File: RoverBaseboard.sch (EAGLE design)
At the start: 57 parts, among them IC3 3.3V, U2 microSD

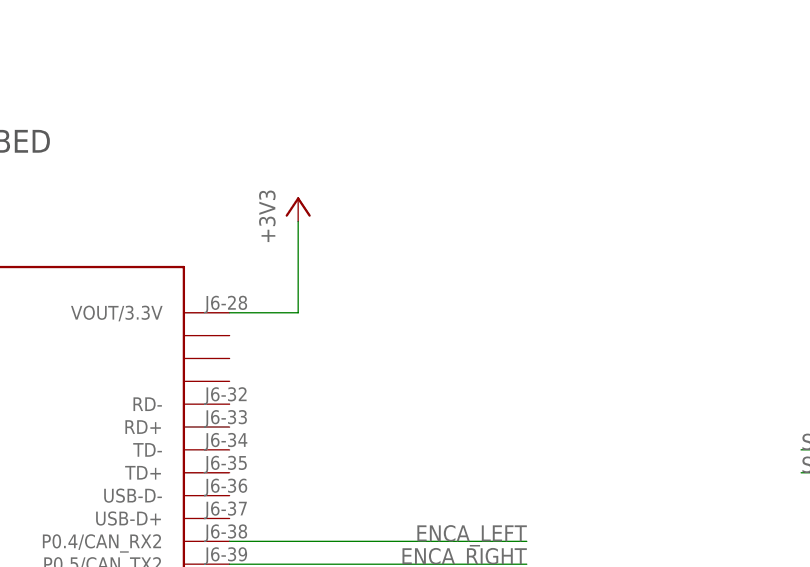
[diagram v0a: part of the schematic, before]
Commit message: added diode for VUSB/5V so both can be connected safely
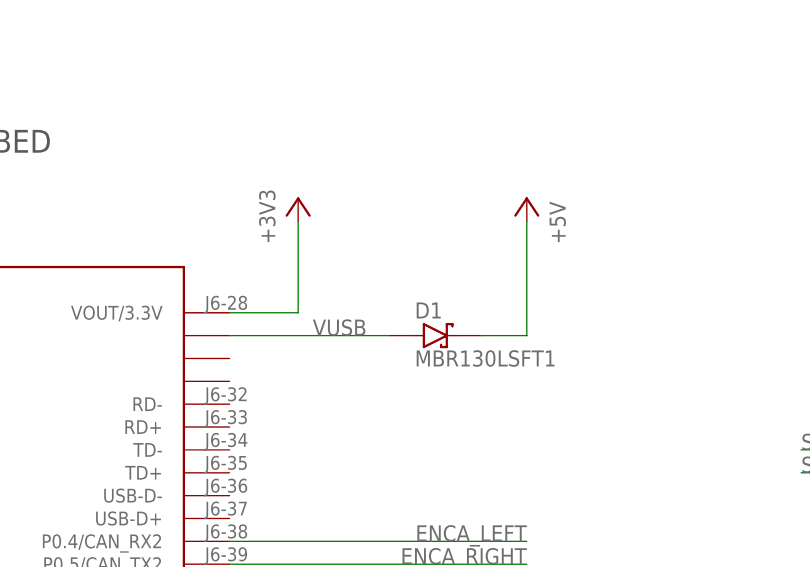
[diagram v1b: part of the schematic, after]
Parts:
- added D1: MBR130LSFT1, bt_diode:SCHOTTKY-DIODE-MBR130LSFT1
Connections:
- new net VUSB: D1.A, U$1.P$26
- net +5V: now also D1.C
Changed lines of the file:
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@@
 <?xml version="1.0" encoding="utf-8"?>
 <!DOCTYPE eagle SYSTEM "eagle.dtd">
-<eagle version="6.4">
+<eagle version="7.1.0">
 <drawing>
 <settings>
@@
 <grid distance="0.1" unitdist="inch" unit="inch" style="lines" multiple="1" display="no" altdistance="0.01" altunitdist="inch" altunit="inch"/>
 <layers>
-<layer number="1" name="Top" color="4" fill="1" visible="yes" active="no"/>
-<layer number="16" name="Bottom" color="1" fill="1" visible="yes" active="no"/>
-<layer number="17" name="Pads" color="2" fill="1" visible="yes" active="no"/>
-<layer number="18" name="Vias" color="2" fill="1" visible="yes" active="no"/>
-<layer number="19" name="Unrouted" color="6" fill="1" visible="yes" active="no"/>
-<layer number="20" name="Dimension" color="15" fill="1" visible="yes" active="no"/>
-<layer number="21" name="tPlace" color="7" fill="1" visible="yes" active="no"/>
-<layer number="22" name="bPlace" color="7" fill="1" visible="yes" active="no"/>
-<layer number="23" name="tOrigins" color="15" fill="1" visible="yes" active="no"/>
-<layer number="24" name="bOrigins" color="15" fill="1" visible="yes" active="no"/>
-<layer number="25" name="tNames" color="7" fill="1" visible="yes" active="no"/>
-<layer number="26" name="bNames" color="7" fill="1" visible="yes" active="no"/>
-<layer number="27" name="tValues" color="7" fill="1" visible="yes" active="no"/>
-<layer number="28" name="bValues" color="7" fill="1" visible="yes" active="no"/>
+<layer number="1" name="Top" color="4" fill="1" visible="no" active="no"/>
+<layer number="16" name="Bottom" color="1" fill="1" visible="no" active="no"/>
+<layer number="17" name="Pads" color="2" fill="1" visible="no" active="no"/>
+<layer number="18" name="Vias" color="2" fill="1" visible="no" active="no"/>
+<layer number="19" name="Unrouted" color="6" fill="1" visible="no" active="no"/>
+<layer number="20" name="Dimension" color="15" fill="1" visible="no" active="no"/>
+<layer number="21" name="tPlace" color="7" fill="1" visible="no" active="no"/>
+<layer number="22" name="bPlace" color="7" fill="1" visible="no" active="no"/>
+<layer number="23" name="tOrigins" color="15" fill="1" visible="no" active="no"/>
+<layer number="24" name="bOrigins" color="15" fill="1" visible="no" active="no"/>
+<layer number="25" name="tNames" color="7" fill="1" visible="no" active="no"/>
+<layer number="26" name="bNames" color="7" fill="1" visible="no" active="no"/>
+<layer number="27" name="tValues" color="7" fill="1" visible="no" active="no"/>
+<layer number="28" name="bValues" color="7" fill="1" visible="no" active="no"/>
 <layer number="29" name="tStop" color="7" fill="3" visible="no" active="no"/>
 <layer number="30" name="bStop" color="7" fill="6" visible="no" active="no"/>
@@
 <layer number="35" name="tGlue" color="7" fill="4" visible="no" active="no"/>
 <layer number="36" name="bGlue" color="7" fill="5" visible="no" active="no"/>
-<layer number="37" name="tTest" color="7" fill="1" visible="yes" active="no"/>
-<layer number="38" name="bTest" color="7" fill="1" visible="yes" active="no"/>
+<layer number="37" name="tTest" color="7" fill="1" visible="no" active="no"/>
+<layer number="38" name="bTest" color="7" fill="1" visible="no" active="no"/>
 <layer number="39" name="tKeepout" color="4" fill="11" visible="no" active="no"/>
 <layer number="40" name="bKeepout" color="1" fill="11" visible="no" active="no"/>
@@
 <layer number="44" name="Drills" color="7" fill="1" visible="no" active="no"/>
 <layer number="45" name="Holes" color="7" fill="1" visible="no" active="no"/>
-<layer number="46" name="Milling" color="3" fill="1" visible="yes" active="no"/>
-<layer number="47" name="Measures" color="7" fill="1" visible="yes" active="no"/>
-<layer number="48" name="Document" color="7" fill="1" visible="yes" active="no"/>
-<layer number="49" name="Reference" color="7" fill="1" visible="yes" active="no"/>
-<layer number="50" name="dxf" color="7" fill="1" visible="yes" active="no"/>
-<layer number="51" name="tDocu" color="7" fill="1" visible="yes" active="no"/>
-<layer number="52" name="bDocu" color="7" fill="1" visible="yes" active="no"/>
-<layer number="53" name="tGND_GNDA" color="7" fill="9" visible="yes" active="no"/>
-<layer number="54" name="bGND_GNDA" color="1" fill="9" visible="yes" active="no"/>
-<layer number="56" name="wert" color="7" fill="1" visible="yes" active="no"/>
+<layer number="46" name="Milling" color="3" fill="1" visible="no" active="no"/>
+<layer number="47" name="Measures" color="7" fill="1" visible="no" active="no"/>
+<layer number="48" name="Document" color="7" fill="1" visible="no" active="no"/>
+<layer number="49" name="Reference" color="7" fill="1" visible="no" active="no"/>
+<layer number="50" name="dxf" color="7" fill="1" visible="no" active="no"/>
+<layer number="51" name="tDocu" color="7" fill="1" visible="no" active="no"/>
+<layer number="52" name="bDocu" color="7" fill="1" visible="no" active="no"/>
+<layer number="53" name="tGND_GNDA" color="7" fill="9" visible="no" active="no"/>
+<layer number="54" name="bGND_GNDA" color="1" fill="9" visible="no" active="no"/>
+<layer number="56" name="wert" color="7" fill="1" visible="no" active="no"/>
 <layer number="91" name="Nets" color="2" fill="1" visible="yes" active="yes"/>
 <layer number="92" name="Busses" color="1" fill="1" visible="yes" active="yes"/>
@@
 <layer number="97" name="Info" color="7" fill="1" visible="yes" active="yes"/>
 <layer number="98" name="Guide" color="6" fill="1" visible="yes" active="yes"/>
+<layer number="99" name="SpiceOrder" color="5" fill="1" visible="yes" active="yes"/>
 <layer number="100" name="Muster" color="7" fill="1" visible="no" active="no"/>
 <layer number="101" name="Hidden" color="15" fill="1" visible="no" active="yes"/>
@@
 </part>
 <part name="SUPPLY13" library="supply2" deviceset="GND" device=""/>
+<part name="D1" library="bt_diode" deviceset="SCHOTTKY-DIODE" device="-MBR130LSFT1" value="MBR130LSFT1"/>
+<part name="P+1" library="supply1" deviceset="+5V" device=""/>
 </parts>
 <sheets>
@@
 </instance>
 <instance part="SUPPLY13" gate="GND" x="416.56" y="50.8"/>
+<instance part="D1" gate="1" x="147.32" y="187.96"/>
+<instance part="P+1" gate="1" x="157.48" y="203.2" rot="MR0"/>
 </instances>
 <busses>
@@
 <pinref part="P+4" gate="1" pin="+5V"/>
 </segment>
+<segment>
+<pinref part="D1" gate="1" pin="C"/>
+<wire x1="152.4" y1="187.96" x2="157.48" y2="187.96" width="0.1524" layer="91"/>
+<wire x1="157.48" y1="187.96" x2="157.48" y2="200.66" width="0.1524" layer="91"/>
+<pinref part="P+1" gate="1" pin="+5V"/>
+</segment>
 </net>
 <net name="+3V3" class="0">
@@
 </segment>
 </net>
+<net name="VUSB" class="0">
+<segment>
+<pinref part="U$1" gate="G$1" pin="P$26"/>
+<wire x1="124.46" y1="187.96" x2="142.24" y2="187.96" width="0.1524" layer="91"/>
+<label x="139.7" y="187.96" size="1.778" layer="95" rot="MR0"/>
+<pinref part="D1" gate="1" pin="A"/>
+</segment>
+</net>
